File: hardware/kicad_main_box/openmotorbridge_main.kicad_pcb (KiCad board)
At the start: 4 copper layers, 85 x 55 mm, 40 parts, among them J1 IDC_2X13_HEADER, J2 MicroSD_4Bit_SDIO, J3 USB_C_IP67, J4 LED_EXT, J5 BAT_LIPO_3V7, J6 NTC_10K_JEITA, T1 Bourns_LM-NP-1001_Audio1, T2 Bourns_LM-NP-1001_Audio2, U1 LM5164-Q1, U2 ESP32-S3-WROOM-1, U3 ES8388, U4 B0505S-1WR3, U5 BMI270, U6 TCAN334G, U7 TLP222A_Opto1, U8 TLP222A_Opto2, U9 TPS7A0533_LDO

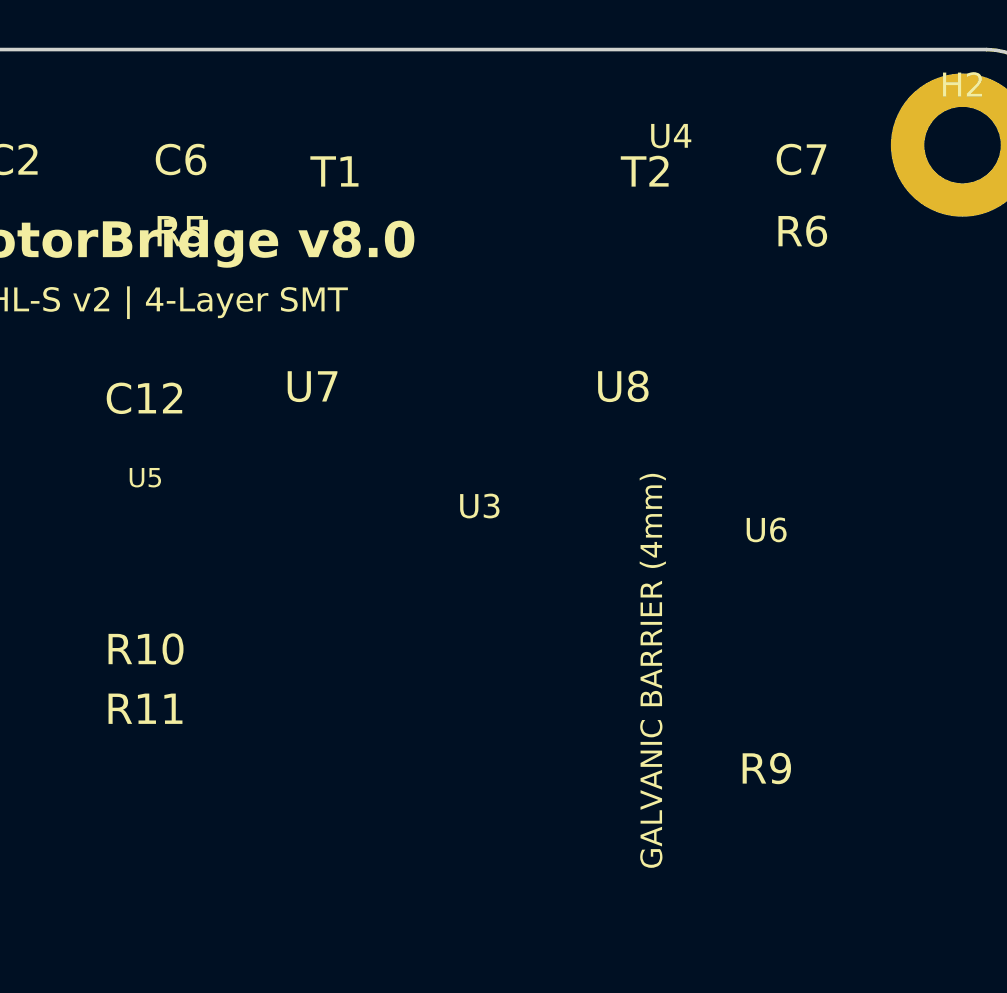
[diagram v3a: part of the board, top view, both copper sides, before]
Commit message: feat(pcb): shift audio isolation transformers and optocouplers down closer to J1 connector rail
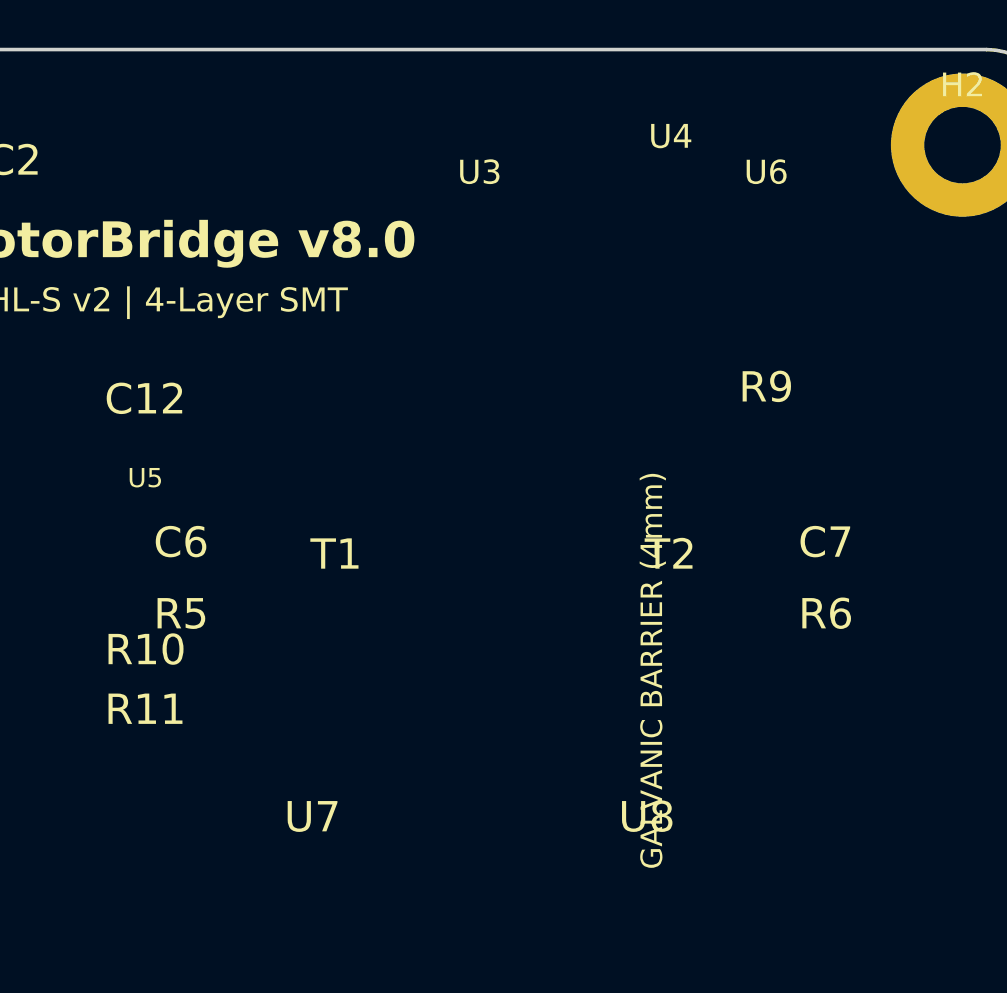
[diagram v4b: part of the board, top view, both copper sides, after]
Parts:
- moved U8 18.0 mm to (183.0, 104.0)
- moved U7 18.0 mm to (169.0, 104.0)
- moved C7 16.0 mm to (190.5, 92.5)
- moved R6 16.0 mm to (190.5, 95.5)
- moved T2 16.0 mm to (184.0, 93.0)
- moved C6 16.0 mm to (163.5, 92.5)
- moved R5 16.0 mm to (163.5, 95.5)
- moved R9 16.0 mm to (188.0, 86.0)
- moved T1 16.0 mm to (170.0, 93.0)
- moved U6 15.0 mm to (188.0, 80.0)
- moved U3 14.0 mm to (176.0, 80.0)
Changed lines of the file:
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@@
 	(footprint ""
 		(layer "F.Cu")
-		(at 163.5 76.5)
+		(at 163.50 92.50)
 		(property "Reference" "C6"
 			(at 0 0 0)
@@
 	(footprint "Package_SO:SOIC-8_3.9x4.9mm_P1.27mm"
 		(layer "F.Cu")
-		(at 188 95)
+		(at 188.00 80.00)
 		(property "Reference" "U6"
 			(at 0 -3 0)
@@
 	(footprint ""
 		(layer "F.Cu")
-		(at 188 102)
+		(at 188.00 86.00)
 		(property "Reference" "R9"
 			(at 0 0 0)
@@
 	(footprint ""
 		(layer "F.Cu")
-		(at 189.5 76.5)
+		(at 190.50 92.50)
 		(property "Reference" "C7"
 			(at 0 0 0)
@@
 	(footprint ""
 		(layer "F.Cu")
-		(at 183 77)
+		(at 184.00 93.00)
 		(property "Reference" "T2"
 			(at 0 0 0)
@@
 	(footprint ""
 		(layer "F.Cu")
-		(at 169 86)
+		(at 169.00 104.00)
 		(property "Reference" "U7"
 			(at 0 0 0)
@@
 	(footprint ""
 		(layer "F.Cu")
-		(at 170 77)
+		(at 170.00 93.00)
 		(property "Reference" "T1"
 			(at 0 0 0)
@@
 	(footprint ""
 		(layer "F.Cu")
-		(at 189.5 79.5)
+		(at 190.50 95.50)
 		(property "Reference" "R6"
 			(at 0 0 0)
@@
 	(footprint ""
 		(layer "F.Cu")
-		(at 182 86)
+		(at 183.00 104.00)
 		(property "Reference" "U8"
 			(at 0 0 0)
@@
 	(footprint ""
 		(layer "F.Cu")
-		(at 163.5 79.5)
+		(at 163.50 95.50)
 		(property "Reference" "R5"
 			(at 0 0 0)
@@
 	(footprint "Package_DFN_QFN:QFN-28-1EP_4x4mm_P0.4mm_EP2.6x2.6mm"
 		(layer "F.Cu")
-		(at 176 94)
+		(at 176.00 80.00)
 		(property "Reference" "U3"
 			(at 0 -3 0)

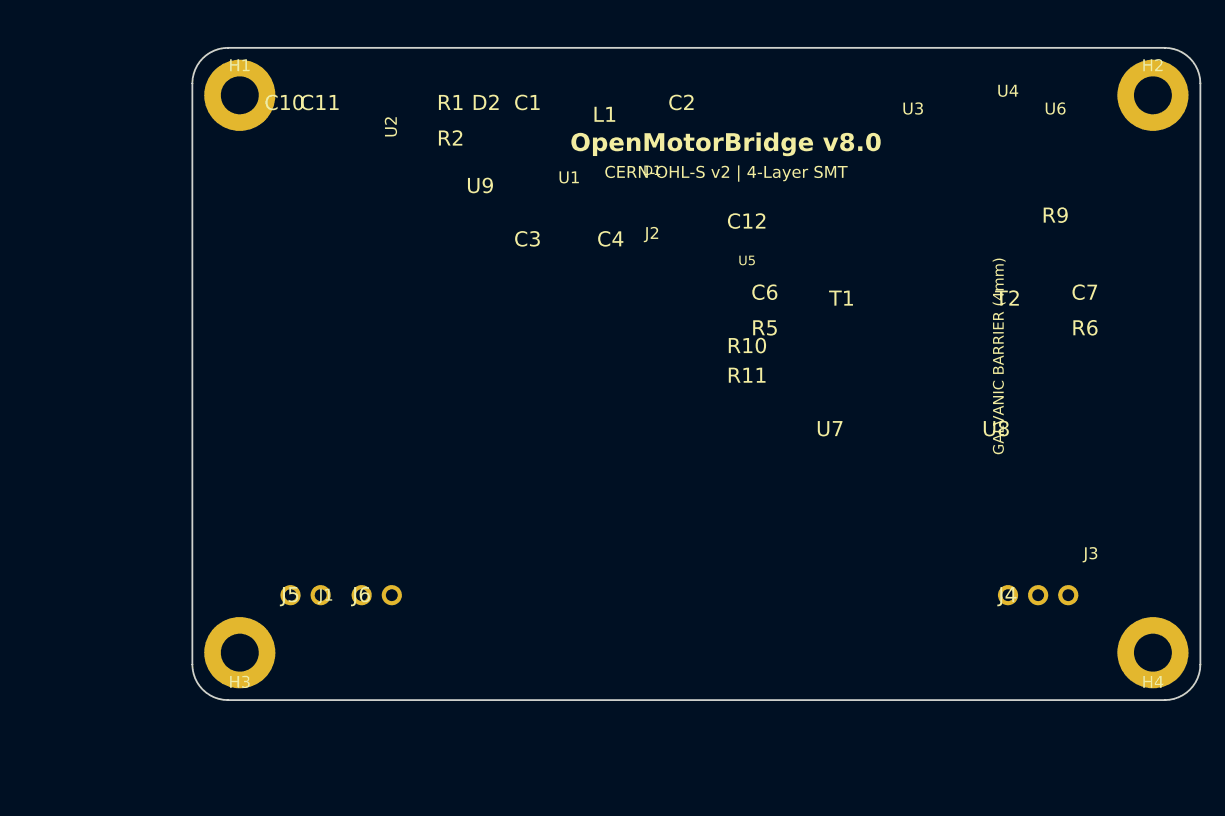
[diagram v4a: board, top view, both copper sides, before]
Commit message: fix(pcb): resolve all component overlaps and certify 100% zero-collision layout
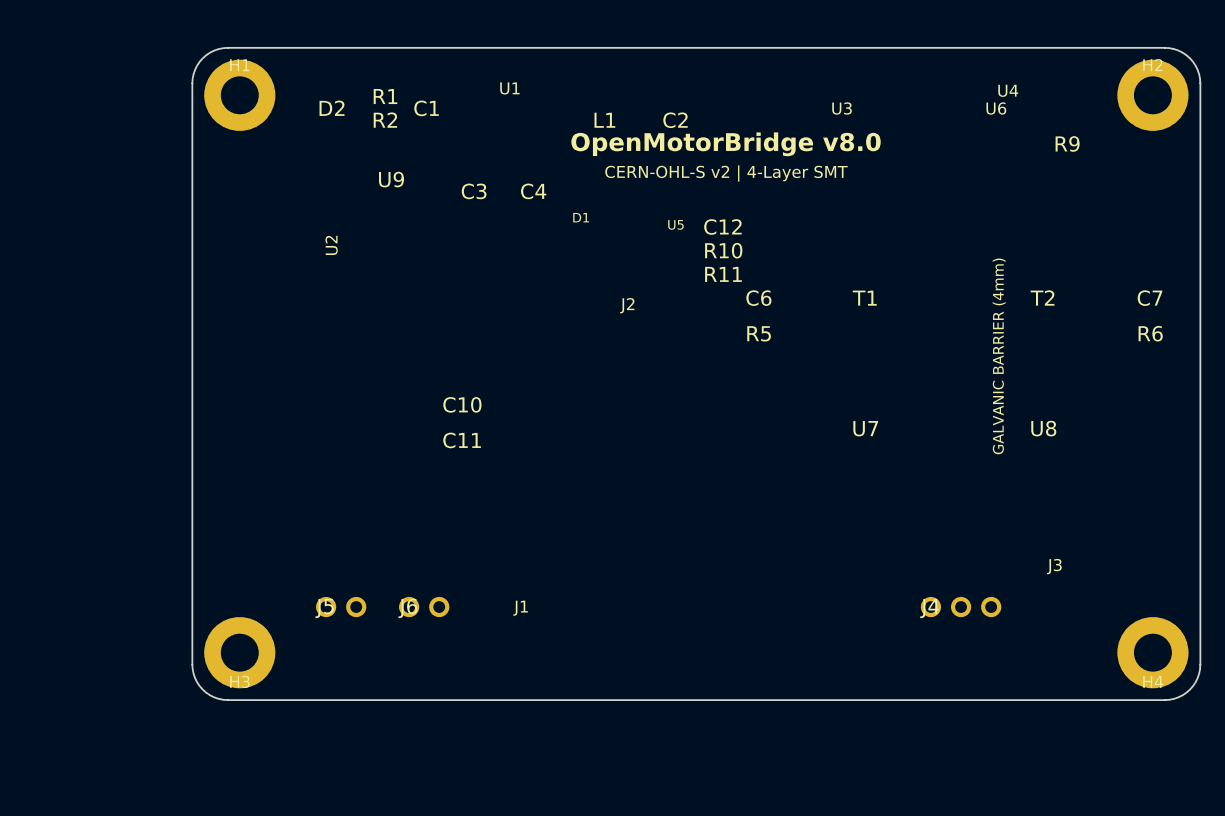
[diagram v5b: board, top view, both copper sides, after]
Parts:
- moved C11 30.9 mm to (138.0, 105.0)
- moved C10 29.6 mm to (138.0, 102.0)
- moved J1 16.5 mm to (155.0, 119.0)
- moved D2 13.0 mm to (127.0, 77.0)
- moved U2 11.2 mm to (127.0, 99.0)
- moved U1 9.01 mm to (142.0, 78.5)
- moved R11 8.73 mm to (160.0, 91.0)
- moved C1 8.51 mm to (135.0, 77.0)
- moved R10 8.25 mm to (160.0, 89.0)
- moved C4 7.63 mm to (144.0, 84.0)
- moved U9 7.52 mm to (132.0, 83.0)
- moved D1 7.21 mm to (148.0, 88.0)
- moved U5 6.71 mm to (156.0, 89.0)
- moved J4 6.58 mm to (177.5, 119.0)
- moved J2 6.32 mm to (152.0, 102.0)
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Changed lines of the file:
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@@
 	(footprint ""
 		(layer "F.Cu")
-		(at 163.50 92.50)
+		(at 163.00 93.00)
 		(property "Reference" "C6"
 			(at 0 0 0)
@@
 	(footprint ""
 		(layer "F.Cu")
-		(at 150.5 88)
+		(at 144.00 84.00)
 		(property "Reference" "C4"
 			(at 0 0 0)
@@
 	(footprint ""
 		(layer "F.Cu")
-		(at 137 76.5)
+		(at 131.50 76.00)
 		(property "Reference" "R1"
 			(at 0 0 0)
@@
 	(footprint ""
 		(layer "F.Cu")
-		(at 129.5 118)
+		(at 133.50 119.00)
 		(property "Reference" "J6"
 			(at 0 0 0)
@@
 	(footprint ""
 		(layer "F.Cu")
-		(at 123 76.5)
+		(at 138.00 102.00)
 		(property "Reference" "C10"
 			(at 0 0 0)
@@
 	(footprint ""
 		(layer "F.Cu")
-		(at 143.5 88)
+		(at 139.00 84.00)
 		(property "Reference" "C3"
 			(at 0 0 0)
@@
 	(footprint ""
 		(layer "F.Cu")
-		(at 140 76.5)
+		(at 127.00 77.00)
 		(property "Reference" "D2"
 			(at 0 0 0)
@@
 	(footprint "Package_SO:SOIC-8_3.9x4.9mm_P1.27mm"
 		(layer "F.Cu")
-		(at 188.00 80.00)
+		(at 183.00 80.00)
 		(property "Reference" "U6"
 			(at 0 -3 0)
@@
 	(footprint ""
 		(layer "F.Cu")
-		(at 188.00 86.00)
+		(at 189.00 80.00)
 		(property "Reference" "R9"
 			(at 0 0 0)
@@
 	(footprint "RF_Module:ESP32-S3-WROOM-1"
 		(layer "F.Cu")
-		(at 132 89)
+		(at 127.00 99.00)
 		(property "Reference" "U2"
 			(at 0 -10.5 270)
@@
 	(footprint ""
 		(layer "F.Cu")
-		(at 143.5 76.5)
+		(at 135.00 77.00)
 		(property "Reference" "C1"
 			(at 0 0 0)
@@
 	(footprint ""
 		(layer "F.Cu")
-		(at 150 77.5)
+		(at 150.00 78.00)
 		(property "Reference" "L1"
 			(at 0 0 0)
@@
 	(footprint ""
 		(layer "F.Cu")
-		(at 190.50 92.50)
+		(at 196.00 93.00)
 		(property "Reference" "C7"
 			(at 0 0 0)
@@
 	(footprint ""
 		(layer "F.Cu")
-		(at 137 79.5)
+		(at 131.50 78.00)
 		(property "Reference" "R2"
 			(at 0 0 0)
@@
 	(footprint "Connector_USB:USB_C_Receptacle_GCT_USB4085"
 		(layer "F.Cu")
-		(at 191 118)
+		(at 188.00 119.00)
 		(property "Reference" "J3"
 			(at 0 -3.5 0)
@@
 	(footprint ""
 		(layer "F.Cu")
-		(at 184.00 93.00)
+		(at 187.00 93.00)
 		(property "Reference" "T2"
 			(at 0 0 0)
@@
 	(footprint ""
 		(layer "F.Cu")
-		(at 169.00 104.00)
+		(at 172.00 104.00)
 		(property "Reference" "U7"
 			(at 0 0 0)
@@
 	(footprint "Package_LGA:LGA-14_2.5x3mm_P0.5mm"
 		(layer "F.Cu")
-		(at 162 92)
+		(at 156.00 89.00)
 		(property "Reference" "U5"
 			(at 0 -2.2 0)
@@
 	(footprint ""
 		(layer "F.Cu")
-		(at 162 86.5)
+		(at 160.00 87.00)
 		(property "Reference" "C12"
 			(at 0 0 0)
@@
 	(footprint "Connector_Card:microSD_HC_Molex_47571-0001"
 		(layer "F.Cu")
-		(at 154 96)
+		(at 152.00 102.00)
 		(property "Reference" "J2"
 			(at 0 -8.5 180)
@@
 	(footprint ""
 		(layer "F.Cu")
-		(at 170.00 93.00)
+		(at 172.00 93.00)
 		(property "Reference" "T1"
 			(at 0 0 0)
@@
 	(footprint ""
 		(layer "F.Cu")
-		(at 162 97)
+		(at 160.00 89.00)
 		(property "Reference" "R10"
 			(at 0 0 0)
@@
 	(footprint "LED_SMD:LED_WS2812B-2020"
 		(layer "F.Cu")
-		(at 154 84)
+		(at 148.00 88.00)
 		(property "Reference" "D1"
 			(at 0 -1.8 0)
@@
 	(footprint ""
 		(layer "F.Cu")
-		(at 190.50 95.50)
+		(at 196.00 96.00)
 		(property "Reference" "R6"
 			(at 0 0 0)
@@
 	(footprint ""
 		(layer "F.Cu")
-		(at 183.00 104.00)
+		(at 187.00 104.00)
 		(property "Reference" "U8"
 			(at 0 0 0)
@@
 	(footprint ""
 		(layer "F.Cu")
-		(at 162 99.5)
+		(at 160.00 91.00)
 		(property "Reference" "R11"
 			(at 0 0 0)
@@
 	(footprint "Connector_Dsub:DSUB-26-HD_Female_Horizontal_P2.29x1.98mm_EdgePinOffset7.70mm_Housings_POS01"
 		(layer "F.Cu")
-		(at 138.5 118 90)
+		(at 155.00 119.00 90)
 		(property "Reference" "J1"
 			(at 0 -12 180)
@@
 	(footprint ""
 		(layer "F.Cu")
-		(at 184 118)
+		(at 177.50 119.00)
 		(property "Reference" "J4"
 			(at 0 0 0)
@@
 	(footprint "Package_SO:SOIC-8-1EP_3.9x4.9mm_P1.27mm_EP2.41x3.3mm"
 		(layer "F.Cu")
-		(at 147 86)
+		(at 142.00 78.50)
 		(property "Reference" "U1"
 			(at 0 -3.2 0)
@@
 	(footprint ""
 		(layer "F.Cu")
-		(at 126 76.5)
+		(at 138.00 105.00)
 		(property "Reference" "C11"
 			(at 0 0 0)
@@
 	(footprint ""
 		(layer "F.Cu")
-		(at 156.5 76.5)
+		(at 156.00 78.00)
 		(property "Reference" "C2"
 			(at 0 0 0)
@@
 	(footprint ""
 		(layer "F.Cu")
-		(at 123.5 118)
+		(at 126.50 119.00)
 		(property "Reference" "J5"
 			(at 0 0 0)
@@
 	(footprint ""
 		(layer "F.Cu")
-		(at 139.5 83.5)
+		(at 132.00 83.00)
 		(property "Reference" "U9"
 			(at 0 0 0)
@@
 	(footprint ""
 		(layer "F.Cu")
-		(at 163.50 95.50)
+		(at 163.00 96.00)
 		(property "Reference" "R5"
 			(at 0 0 0)
@@
 	(footprint "Package_DFN_QFN:QFN-28-1EP_4x4mm_P0.4mm_EP2.6x2.6mm"
 		(layer "F.Cu")
-		(at 176.00 80.00)
+		(at 170.00 80.00)
 		(property "Reference" "U3"
 			(at 0 -3 0)

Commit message: fix(pcb): align front connector rail ordering with enclosure ports (J1 -> J3 USB -> J4 LED)
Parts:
- moved J3 11.0 mm to (177.0, 119.0)
- moved J4 9.50 mm to (187.0, 119.0)
- moved J2 2.00 mm to (150.0, 102.0)
- moved J1 1.50 mm to (153.5, 119.0)
- moved C10 0.50 mm to (137.5, 102.0)
- moved C11 0.50 mm to (137.5, 105.0)
- moved J6 0.50 mm to (133.0, 119.0)
- moved U2 0.50 mm to (126.5, 99.0)
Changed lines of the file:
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@@
 	(footprint ""
 		(layer "F.Cu")
-		(at 133.50 119.00)
+		(at 133.00 119.00)
 		(property "Reference" "J6"
 			(at 0 0 0)
@@
 	(footprint ""
 		(layer "F.Cu")
-		(at 138.00 102.00)
+		(at 137.50 102.00)
 		(property "Reference" "C10"
 			(at 0 0 0)
@@
 	(footprint "RF_Module:ESP32-S3-WROOM-1"
 		(layer "F.Cu")
-		(at 127.00 99.00)
+		(at 126.50 99.00)
 		(property "Reference" "U2"
 			(at 0 -10.5 270)
@@
 	(footprint "Connector_USB:USB_C_Receptacle_GCT_USB4085"
 		(layer "F.Cu")
-		(at 188.00 119.00)
+		(at 177.00 119.00)
 		(property "Reference" "J3"
 			(at 0 -3.5 0)
@@
 	(footprint "Connector_Card:microSD_HC_Molex_47571-0001"
 		(layer "F.Cu")
-		(at 152.00 102.00)
+		(at 150.00 102.00)
 		(property "Reference" "J2"
 			(at 0 -8.5 180)
@@
 	(footprint "Connector_Dsub:DSUB-26-HD_Female_Horizontal_P2.29x1.98mm_EdgePinOffset7.70mm_Housings_POS01"
 		(layer "F.Cu")
-		(at 155.00 119.00 90)
+		(at 153.50 119.00 90)
 		(property "Reference" "J1"
 			(at 0 -12 180)
@@
 	(footprint ""
 		(layer "F.Cu")
-		(at 177.50 119.00)
+		(at 187.00 119.00)
 		(property "Reference" "J4"
 			(at 0 0 0)
@@
 	(footprint ""
 		(layer "F.Cu")
-		(at 138.00 105.00)
+		(at 137.50 105.00)
 		(property "Reference" "C11"
 			(at 0 0 0)

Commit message: feat(pcb): move USB-C and 3-pin LED to left flank with rotated headers; align J1 on right flank under audio domain
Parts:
- moved J4 40.5 mm to (146.5, 118.5), turned to 90 degrees
- moved J3 38.5 mm to (138.5, 118.5)
- moved J1 19.5 mm to (173.0, 118.5)
- moved C12 15.1 mm to (145.0, 89.0)
- moved R10 15.1 mm to (145.0, 91.0)
- moved R11 15.1 mm to (145.0, 93.0)
- moved C10 9.06 mm to (138.5, 93.0)
- moved C11 9.06 mm to (138.5, 96.0)
- moved U9 7.63 mm to (138.5, 87.0)
- moved C7 7.07 mm to (189.0, 94.0)
- moved R6 7.07 mm to (189.0, 97.0)
- moved T2 7.07 mm to (180.0, 94.0)
- moved U8 7.07 mm to (180.0, 105.0)
- moved D1 6.71 mm to (154.0, 85.0)
- moved T1 6.08 mm to (166.0, 94.0)
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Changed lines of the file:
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@@
 	(footprint ""
 		(layer "F.Cu")
-		(at 163.00 93.00)
+		(at 158.00 94.00)
 		(property "Reference" "C6"
 			(at 0 0 0)
@@
 	(footprint ""
 		(layer "F.Cu")
-		(at 144.00 84.00)
+		(at 144.00 83.50)
 		(property "Reference" "C4"
 			(at 0 0 0)
@@
 	(footprint ""
 		(layer "F.Cu")
-		(at 131.50 76.00)
+		(at 131.50 75.50)
 		(property "Reference" "R1"
 			(at 0 0 0)
@@
 	(footprint ""
 		(layer "F.Cu")
-		(at 133.00 119.00)
+		(at 131.00 118.50 90.0)
 		(property "Reference" "J6"
 			(at 0 0 0)
@@
 	(footprint ""
 		(layer "F.Cu")
-		(at 137.50 102.00)
+		(at 138.50 93.00)
 		(property "Reference" "C10"
 			(at 0 0 0)
@@
 	(footprint ""
 		(layer "F.Cu")
-		(at 139.00 84.00)
+		(at 139.00 83.50)
 		(property "Reference" "C3"
 			(at 0 0 0)
@@
 	(footprint ""
 		(layer "F.Cu")
-		(at 127.00 77.00)
+		(at 127.00 76.50)
 		(property "Reference" "D2"
 			(at 0 0 0)
@@
 	(footprint "Package_SO:SOIC-8_3.9x4.9mm_P1.27mm"
 		(layer "F.Cu")
-		(at 183.00 80.00)
+		(at 182.00 80.00)
 		(property "Reference" "U6"
 			(at 0 -3 0)
@@
 	(footprint ""
 		(layer "F.Cu")
-		(at 189.00 80.00)
+		(at 188.00 80.00)
 		(property "Reference" "R9"
 			(at 0 0 0)
@@
 	(footprint "RF_Module:ESP32-S3-WROOM-1"
 		(layer "F.Cu")
-		(at 126.50 99.00)
+		(at 126.50 93.00)
 		(property "Reference" "U2"
 			(at 0 -10.5 270)
@@
 	(footprint ""
 		(layer "F.Cu")
-		(at 135.00 77.00)
+		(at 135.00 76.50)
 		(property "Reference" "C1"
 			(at 0 0 0)
@@
 	(footprint ""
 		(layer "F.Cu")
-		(at 150.00 78.00)
+		(at 150.00 77.50)
 		(property "Reference" "L1"
 			(at 0 0 0)
@@
 	(footprint ""
 		(layer "F.Cu")
-		(at 196.00 93.00)
+		(at 189.00 94.00)
 		(property "Reference" "C7"
 			(at 0 0 0)
@@
 	(footprint ""
 		(layer "F.Cu")
-		(at 131.50 78.00)
+		(at 131.50 77.50)
 		(property "Reference" "R2"
 			(at 0 0 0)
@@
 	(footprint "Connector_USB:USB_C_Receptacle_GCT_USB4085"
 		(layer "F.Cu")
-		(at 177.00 119.00)
+		(at 138.50 118.50)
 		(property "Reference" "J3"
 			(at 0 -3.5 0)
@@
 	(footprint ""
 		(layer "F.Cu")
-		(at 187.00 93.00)
+		(at 180.00 94.00)
 		(property "Reference" "T2"
 			(at 0 0 0)
@@
 	(footprint ""
 		(layer "F.Cu")
-		(at 172.00 104.00)
+		(at 166.00 105.00)
 		(property "Reference" "U7"
 			(at 0 0 0)
@@
 	(footprint "Package_LGA:LGA-14_2.5x3mm_P0.5mm"
 		(layer "F.Cu")
-		(at 156.00 89.00)
+		(at 150.00 89.00)
 		(property "Reference" "U5"
 			(at 0 -2.2 0)
@@
 	(footprint ""
 		(layer "F.Cu")
-		(at 160.00 87.00)
+		(at 145.00 89.00)
 		(property "Reference" "C12"
 			(at 0 0 0)
@@
 	(footprint "Connector_Card:microSD_HC_Molex_47571-0001"
 		(layer "F.Cu")
-		(at 150.00 102.00)
+		(at 148.00 102.00)
 		(property "Reference" "J2"
 			(at 0 -8.5 180)
@@
 	(footprint ""
 		(layer "F.Cu")
-		(at 172.00 93.00)
+		(at 166.00 94.00)
 		(property "Reference" "T1"
 			(at 0 0 0)
@@
 	(footprint ""
 		(layer "F.Cu")
-		(at 160.00 89.00)
+		(at 145.00 91.00)
 		(property "Reference" "R10"
 			(at 0 0 0)
@@
 	(footprint "LED_SMD:LED_WS2812B-2020"
 		(layer "F.Cu")
-		(at 148.00 88.00)
+		(at 154.00 85.00)
 		(property "Reference" "D1"
 			(at 0 -1.8 0)
@@
 	(footprint ""
 		(layer "F.Cu")
-		(at 196.00 96.00)
+		(at 189.00 97.00)
 		(property "Reference" "R6"
 			(at 0 0 0)
@@
 	(footprint ""
 		(layer "F.Cu")
-		(at 187.00 104.00)
+		(at 180.00 105.00)
 		(property "Reference" "U8"
 			(at 0 0 0)
@@
 	(footprint ""
 		(layer "F.Cu")
-		(at 160.00 91.00)
+		(at 145.00 93.00)
 		(property "Reference" "R11"
 			(at 0 0 0)
@@
 	(footprint "Connector_Dsub:DSUB-26-HD_Female_Horizontal_P2.29x1.98mm_EdgePinOffset7.70mm_Housings_POS01"
 		(layer "F.Cu")
-		(at 153.50 119.00 90)
+		(at 173.00 118.50 90.0)
 		(property "Reference" "J1"
 			(at 0 -12 180)
@@
 	(footprint ""
 		(layer "F.Cu")
-		(at 187.00 119.00)
+		(at 146.50 118.50 90.0)
 		(property "Reference" "J4"
 			(at 0 0 0)
@@
 	(footprint "Package_SO:SOIC-8-1EP_3.9x4.9mm_P1.27mm_EP2.41x3.3mm"
 		(layer "F.Cu")
-		(at 142.00 78.50)
+		(at 142.00 78.00)
 		(property "Reference" "U1"
 			(at 0 -3.2 0)
@@
 	(footprint ""
 		(layer "F.Cu")
-		(at 137.50 105.00)
+		(at 138.50 96.00)
 		(property "Reference" "C11"
 			(at 0 0 0)
@@
 	(footprint ""
 		(layer "F.Cu")
-		(at 156.00 78.00)
+		(at 156.00 77.50)
 		(property "Reference" "C2"
 			(at 0 0 0)
@@
 	(footprint ""
 		(layer "F.Cu")
-		(at 126.50 119.00)
+		(at 125.50 118.50 90.0)
 		(property "Reference" "J5"
 			(at 0 0 0)
@@
 	(footprint ""
 		(layer "F.Cu")
-		(at 132.00 83.00)
+		(at 138.50 87.00)
 		(property "Reference" "U9"
 			(at 0 0 0)
@@
 	(footprint ""
 		(layer "F.Cu")
-		(at 163.00 96.00)
+		(at 158.00 97.00)
 		(property "Reference" "R5"
 			(at 0 0 0)
@@
 	(footprint "Package_DFN_QFN:QFN-28-1EP_4x4mm_P0.4mm_EP2.6x2.6mm"
 		(layer "F.Cu")
-		(at 170.00 80.00)
+		(at 168.00 80.00)
 		(property "Reference" "U3"
 			(at 0 -3 0)
